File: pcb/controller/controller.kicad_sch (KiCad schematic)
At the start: 10 parts, among them J1 Joystick-1, J2 Joystick-2, J3 OLED Display, SW1 SW_DIP_x01, U2 UA78M05QDCYRQ1, U3 RFM95W-868S2

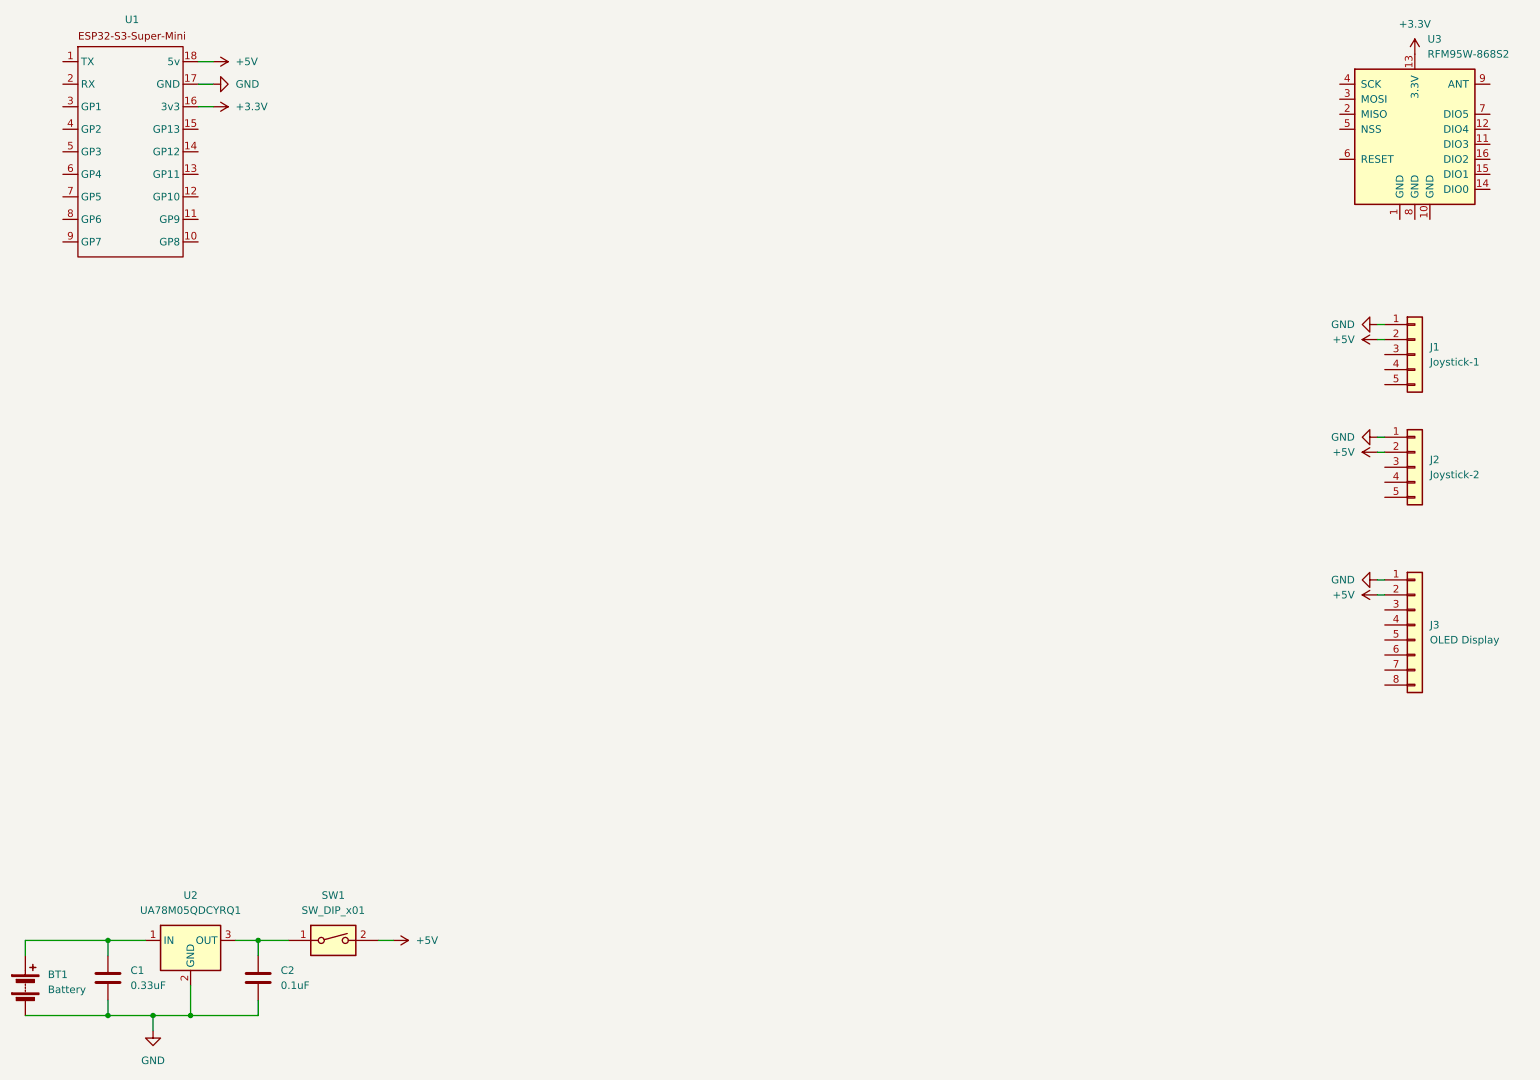
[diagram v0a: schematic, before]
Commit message: switched to node mcu
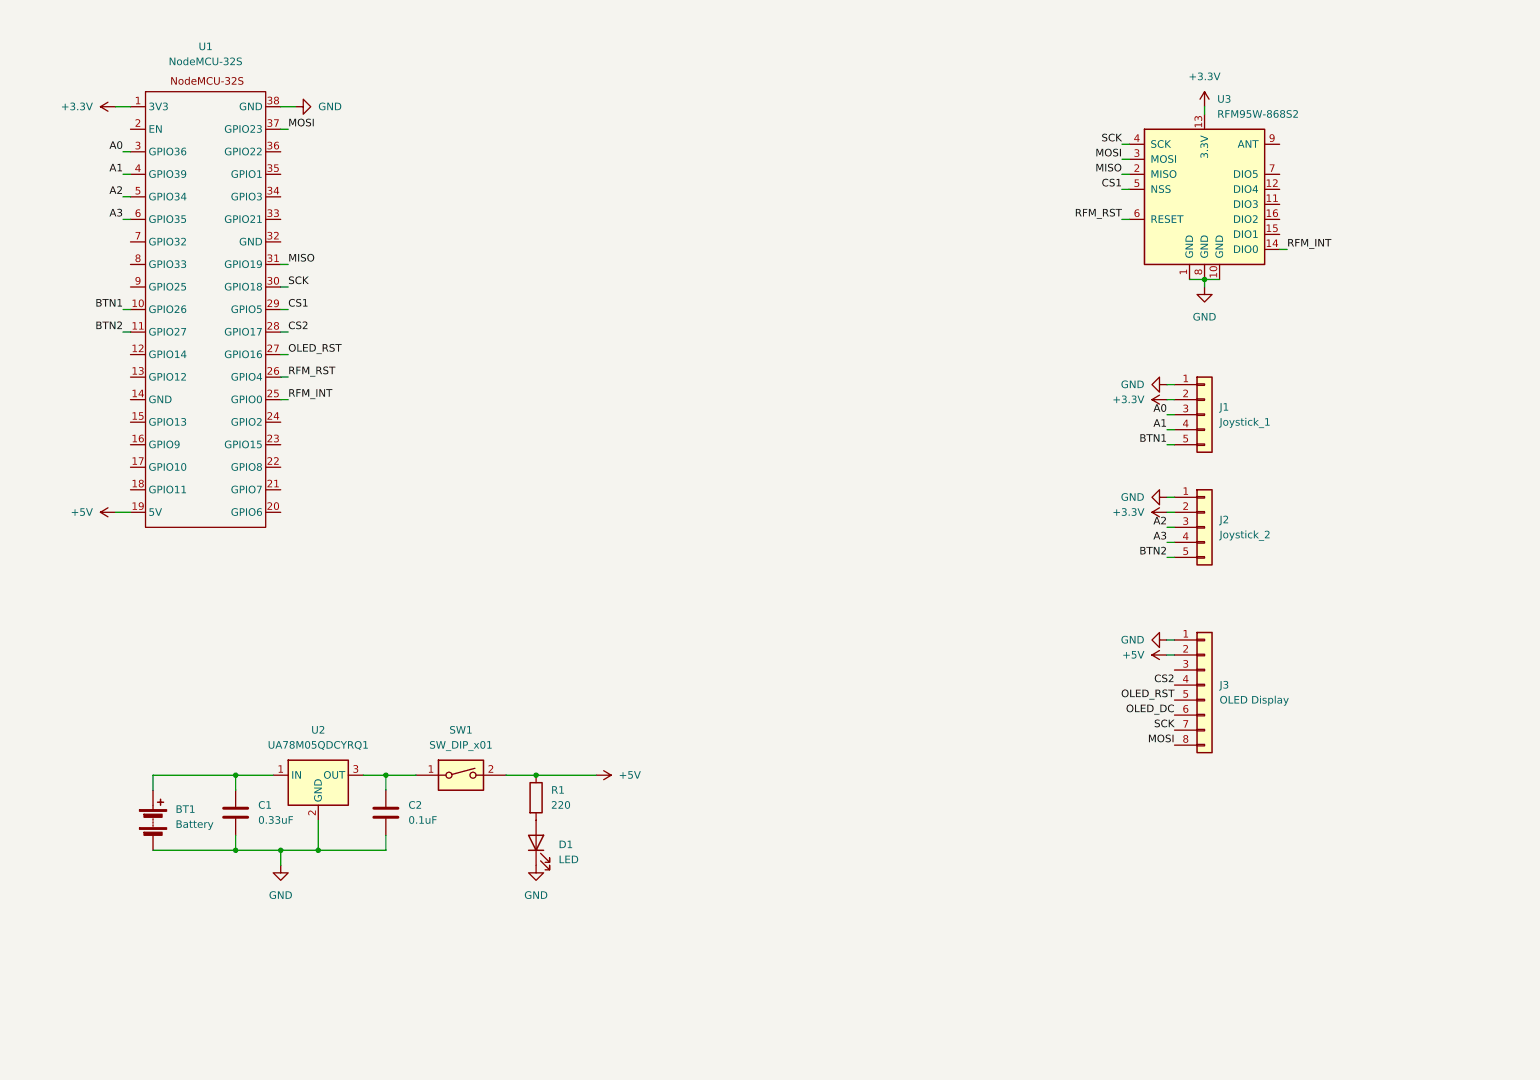
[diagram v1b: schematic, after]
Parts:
- removed U1: ~, symbol controller-library:ESP32-S3-Super-Mini
- added D1: LED, LED_THT:LED_D5.0mm, symbol Device:LED
- added R1: 220, Resistor_SMD:R_0603_1608Metric_Pad0.98x0.95mm_HandSolder, symbol Device:R
- added U1: NodeMCU-32S, controller:NodeMCU-32S, symbol controller-library:NodeMCU-32S
- BT1, SW1: footprint (none) -> Connector_PinHeader_2.54mm:PinHeader_1x02_P2.54mm_Vertical
- C1, C2: footprint (none) -> Capacitor_SMD:C_0603_1608Metric_Pad1.08x0.95mm_HandSolder
- J1: value Joystick-1 -> Joystick_1; footprint (none) -> Connector_PinHeader_2.54mm:PinHeader_1x05_P2.54mm_Vertical
- J2: value Joystick-2 -> Joystick_2; footprint (none) -> Connector_PinHeader_2.54mm:PinHeader_1x05_P2.54mm_Vertical
- J3: footprint (none) -> Connector_PinHeader_2.54mm:PinHeader_1x08_P2.54mm_Vertical
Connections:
- net +3.3V: now also J1.2 (Pin_2), J2.2 (Pin_2), U1.1 (3V3)
- net +5V: now also R1.1, U1.19 (5V); no longer J1.2 (Pin_2), J2.2 (Pin_2)
- net GND: now also U3.1 (GND), U3.10 (GND), U3.8 (GND), D1.1 (K), U1.38 (GND)
- net CS2: now reaches J3.4 (Pin_4)
- net CS2: now also U1.28 (GPIO17)
- net OLED_RST: now reaches J3.5 (Pin_5)
- net OLED_RST: now also U1.27 (GPIO16)
- net OLED_DC: now reaches J3.6 (Pin_6)
- net SCK: now reaches J3.7 (Pin_7)
- net SCK: now also U3.4 (SCK), U1.30 (GPIO18)
- net MOSI: now reaches J3.8 (Pin_8)
- net MOSI: now also U3.3 (MOSI), U1.37 (GPIO23)
- net A2: now reaches J2.3 (Pin_3)
- net A2: now also U1.5 (GPIO34)
- net A3: now reaches J2.4 (Pin_4)
- net A3: now also U1.6 (GPIO35)
- net BTN2: now reaches J2.5 (Pin_5)
- net BTN2: now also U1.11 (GPIO27)
- net A0: now reaches J1.3 (Pin_3)
- net A0: now also U1.3 (GPIO36)
- net A1: now reaches J1.4 (Pin_4)
- net A1: now also U1.4 (GPIO39)
- net BTN1: now reaches J1.5 (Pin_5)
- net BTN1: now also U1.10 (GPIO26)
- net RFM_INT: now reaches U3.14 (DIO0)
- net RFM_INT: now also U1.25 (GPIO0)
- net MISO: now reaches U3.2 (MISO)
- net MISO: now also U1.31 (GPIO19)
- net CS1: now reaches U3.5 (NSS)
- net CS1: now also U1.29 (GPIO5)
- net RFM_RST: now reaches U3.6 (RESET)
- net RFM_RST: now also U1.26 (GPIO4)
- new net: D1.2 (A), R1.2
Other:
- moved on the sheet: BT1, C1, C2, J1, J2, J3, SW1, U2, U3
